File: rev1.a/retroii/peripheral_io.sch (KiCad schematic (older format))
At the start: 8 parts, among them J12 Peripheral Slot 0, J15 Peripheral Slot 4, J16 Peripheral Slot 1, J17 Peripheral Slot 5, J18 Peripheral Slot 2, J19 Peripheral Slot 6, J20 Peripheral Slot 3, J21 Peripheral Slot 7

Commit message: added card edge peripheral connector footprint and 3d model.
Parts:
- J12, J15, J16, J17, J18, J19, J20, J21: footprint (none) -> retroii_footprints:TE_5530841-5
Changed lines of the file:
@@
 F 0 "J12" H 3290 3515 50  0000 C CNN
 F 1 "Peripheral Slot 0" H 3140 915 50  0000 C CNN
-F 2 "" H 3160 2225 50  0001 C CNN
+F 2 "retroii_footprints:TE_5530841-5" H 3160 2225 50  0001 C CNN
 F 3 "~" H 3160 2225 50  0001 C CNN
 	1    3160 2225
@@
 F 0 "J16" H 4975 3515 50  0000 C CNN
 F 1 "Peripheral Slot 1" H 4825 915 50  0000 C CNN
-F 2 "" H 4845 2225 50  0001 C CNN
+F 2 "retroii_footprints:TE_5530841-5" H 4845 2225 50  0001 C CNN
 F 3 "~" H 4845 2225 50  0001 C CNN
 	1    4845 2225
@@
 F 0 "J18" H 6665 3515 50  0000 C CNN
 F 1 "Peripheral Slot 2" H 6515 915 50  0000 C CNN
-F 2 "" H 6535 2225 50  0001 C CNN
+F 2 "retroii_footprints:TE_5530841-5" H 6535 2225 50  0001 C CNN
 F 3 "~" H 6535 2225 50  0001 C CNN
 	1    6535 2225
@@
 F 0 "J20" H 8350 3515 50  0000 C CNN
 F 1 "Peripheral Slot 3" H 8200 915 50  0000 C CNN
-F 2 "" H 8220 2225 50  0001 C CNN
+F 2 "retroii_footprints:TE_5530841-5" H 8220 2225 50  0001 C CNN
 F 3 "~" H 8220 2225 50  0001 C CNN
 	1    8220 2225
@@
 F 0 "J15" H 3290 6390 50  0000 C CNN
 F 1 "Peripheral Slot 4" H 3140 3790 50  0000 C CNN
-F 2 "" H 3160 5100 50  0001 C CNN
+F 2 "retroii_footprints:TE_5530841-5" H 3160 5100 50  0001 C CNN
 F 3 "~" H 3160 5100 50  0001 C CNN
 	1    3160 5100
@@
 F 0 "J17" H 4975 6390 50  0000 C CNN
 F 1 "Peripheral Slot 5" H 4825 3790 50  0000 C CNN
-F 2 "" H 4845 5100 50  0001 C CNN
+F 2 "retroii_footprints:TE_5530841-5" H 4845 5100 50  0001 C CNN
 F 3 "~" H 4845 5100 50  0001 C CNN
 	1    4845 5100
@@
 F 0 "J19" H 6665 6390 50  0000 C CNN
 F 1 "Peripheral Slot 6" H 6515 3790 50  0000 C CNN
-F 2 "" H 6535 5100 50  0001 C CNN
+F 2 "retroii_footprints:TE_5530841-5" H 6535 5100 50  0001 C CNN
 F 3 "~" H 6535 5100 50  0001 C CNN
 	1    6535 5100
@@
 F 0 "J21" H 8350 6390 50  0000 C CNN
 F 1 "Peripheral Slot 7" H 8200 3790 50  0000 C CNN
-F 2 "" H 8220 5100 50  0001 C CNN
+F 2 "retroii_footprints:TE_5530841-5" H 8220 5100 50  0001 C CNN
 F 3 "~" H 8220 5100 50  0001 C CNN
 	1    8220 5100

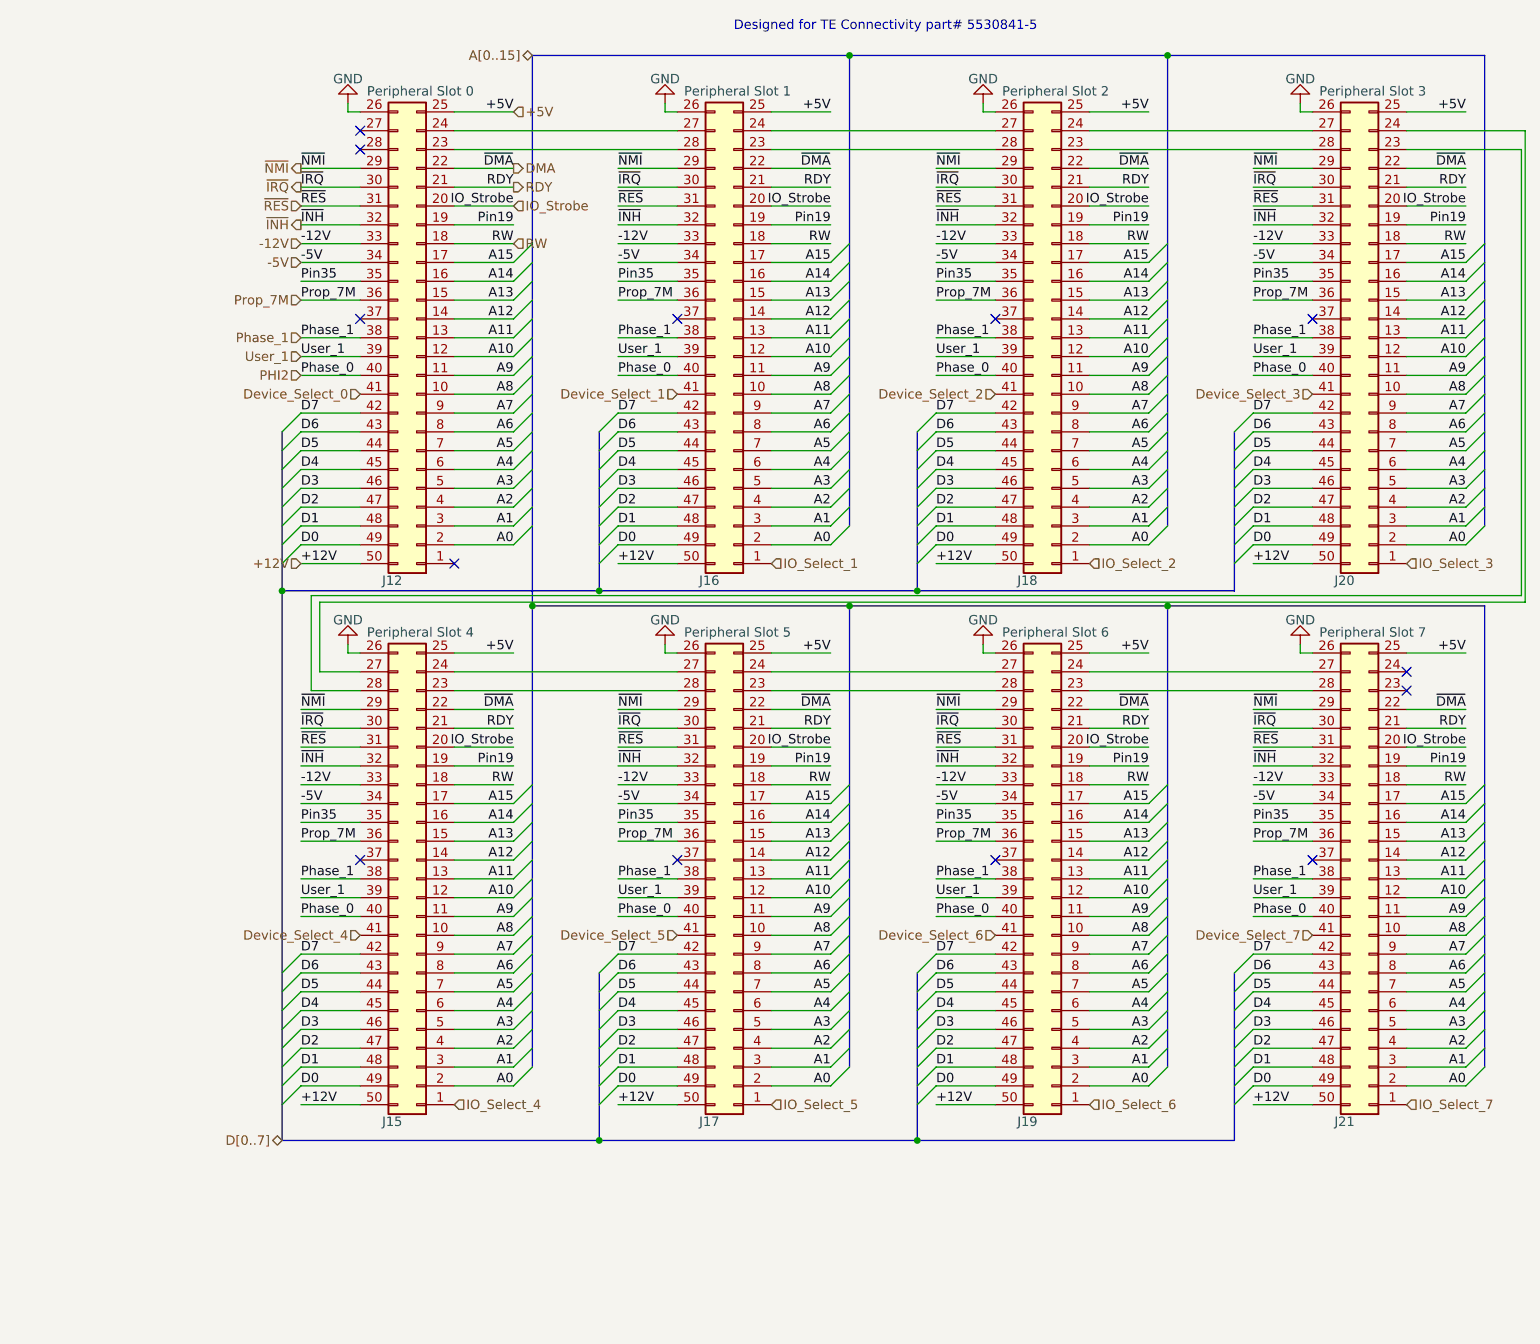
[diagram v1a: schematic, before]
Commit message: added optional bypass caps for peripheral slots
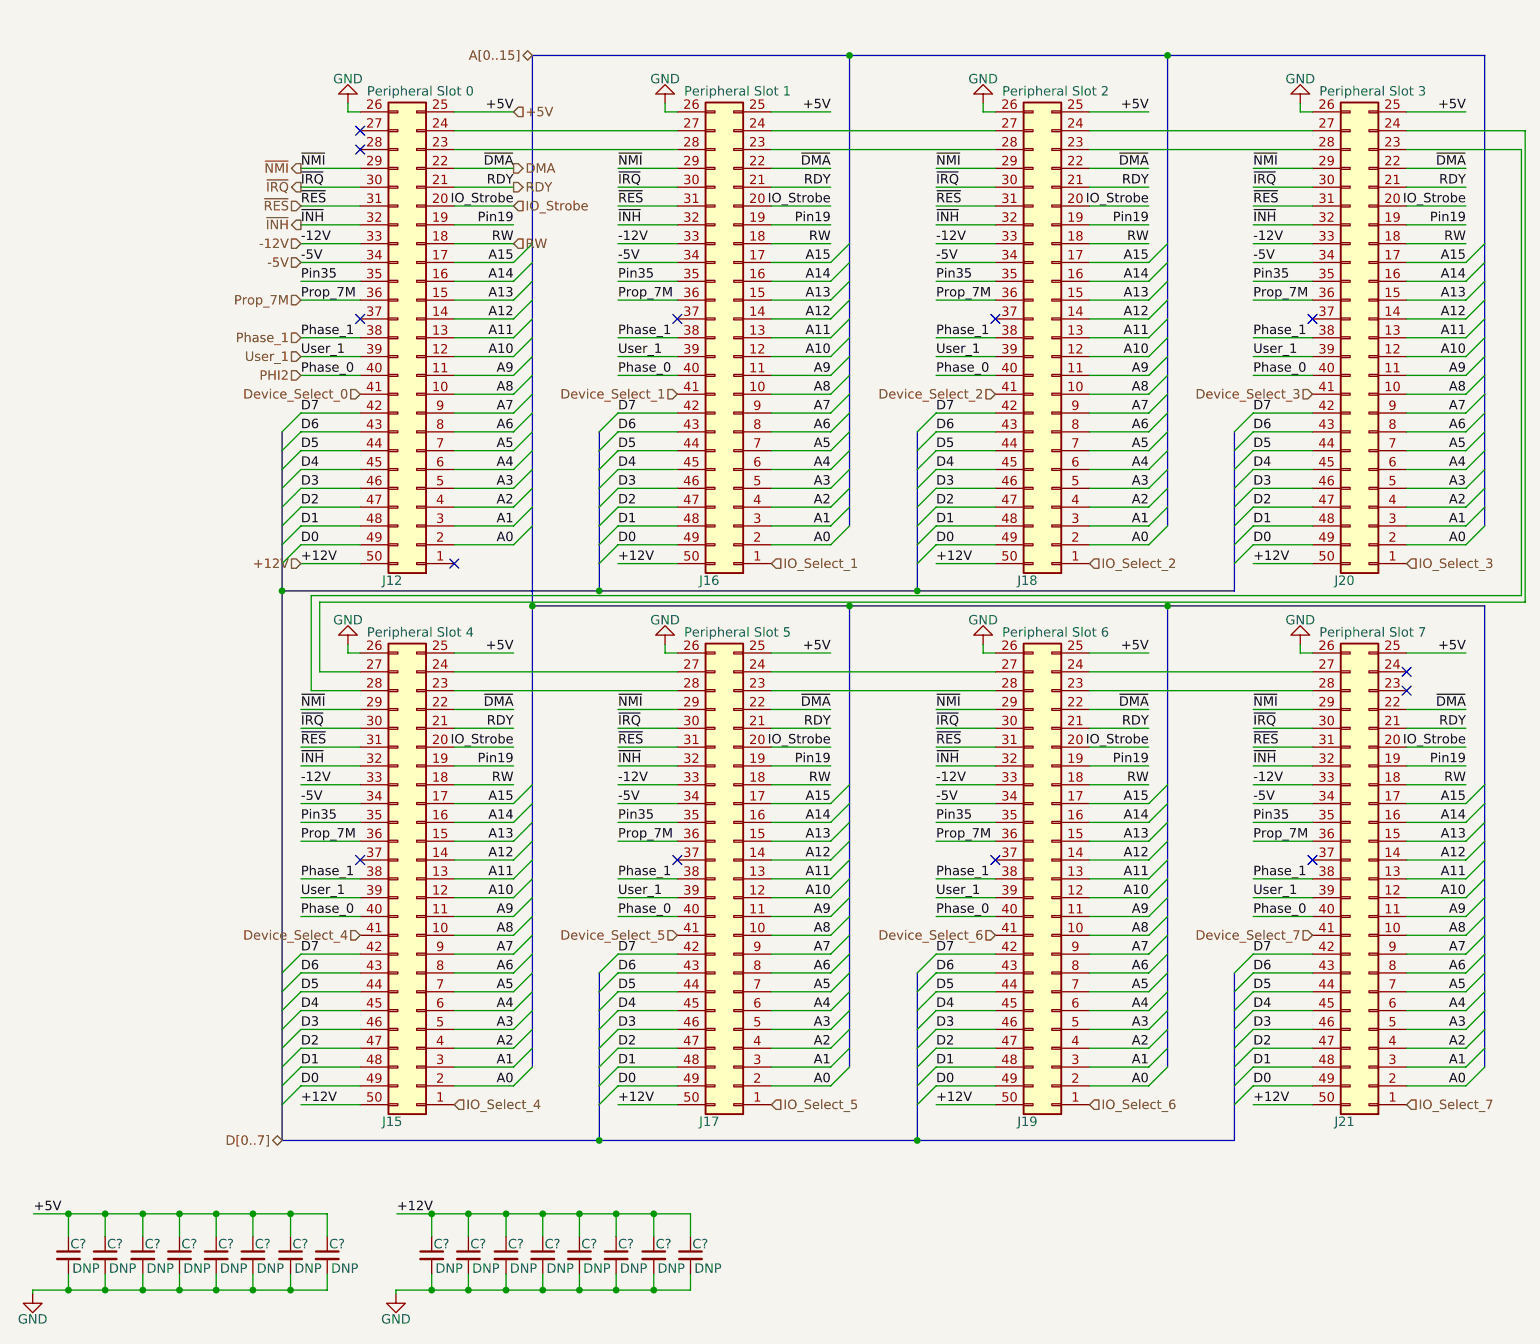
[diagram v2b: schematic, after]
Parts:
- added C? (x16): DNP, symbol Device:C_Small
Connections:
- net +12V: now also C?.1, C?.1, C?.1, C?.1, C?.1, C?.1, C?.1, C?.1
- net +5V: now also C?.1, C?.1, C?.1, C?.1, C?.1, C?.1, C?.1, C?.1
- net GND: now also C?.2, C?.2, C?.2, C?.2, C?.2, C?.2, C?.2, C?.2, C?.2, C?.2, C?.2, C?.2, C?.2, C?.2, C?.2, C?.2
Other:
- note removed: "Designed for TE Connectivity part# 5530841-5"

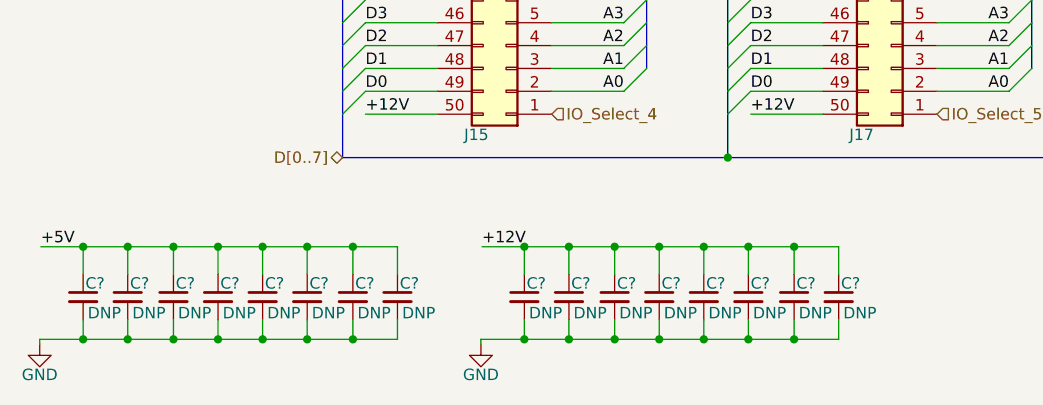
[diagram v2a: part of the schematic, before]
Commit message: added vga dsub-15 footprint and 3d model
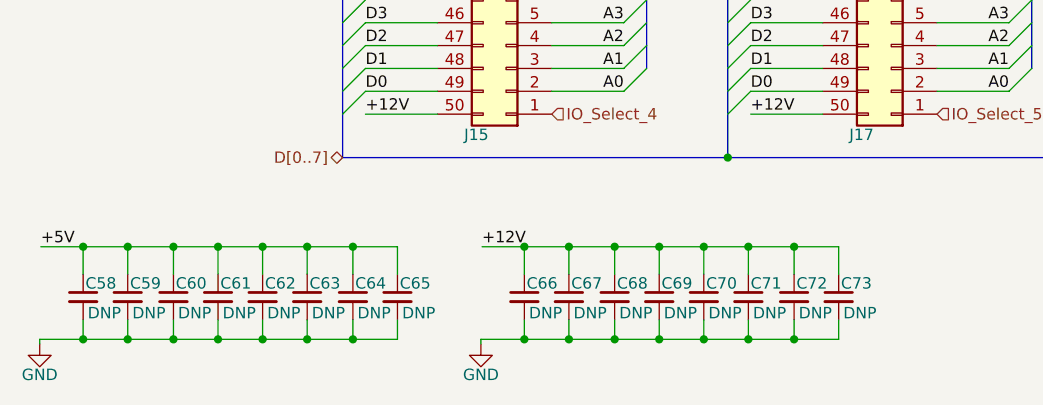
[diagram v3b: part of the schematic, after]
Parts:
- C58, C59, C60, C61, C62, C63, C64, C65, C66, C67, C68, C69, C70, C71, C72, C73: renamed from C?; footprint (none) -> retroii_footprints:C_Disc_D3.0mm_W2.0mm_P2.50mm
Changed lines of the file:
@@
 Prop_7M
 $Comp
-L Device:C_Small C?
+L Device:C_Small C58
 U 1 1 5CD43AB0
 P 1310 7100
-F 0 "C?" H 1320 7160 50  0000 L CNN
+F 0 "C58" H 1320 7160 50  0000 L CNN
 F 1 "DNP" H 1330 7030 50  0000 L CNN
-F 2 "" H 1310 7100 50  0001 C CNN
+F 2 "retroii_footprints:C_Disc_D3.0mm_W2.0mm_P2.50mm" H 1310 7100 50  0001 C CNN
 F 3 "~" H 1310 7100 50  0001 C CNN
 	1    1310 7100
@@
 $EndComp
 $Comp
-L Device:C_Small C?
+L Device:C_Small C59
 U 1 1 5CD476D4
 P 1505 7100
-F 0 "C?" H 1515 7160 50  0000 L CNN
+F 0 "C59" H 1515 7160 50  0000 L CNN
 F 1 "DNP" H 1525 7030 50  0000 L CNN
-F 2 "" H 1505 7100 50  0001 C CNN
+F 2 "retroii_footprints:C_Disc_D3.0mm_W2.0mm_P2.50mm" H 1505 7100 50  0001 C CNN
 F 3 "~" H 1505 7100 50  0001 C CNN
 	1    1505 7100
@@
 $EndComp
 $Comp
-L Device:C_Small C?
+L Device:C_Small C60
 U 1 1 5CD4865B
 P 1705 7100
-F 0 "C?" H 1715 7160 50  0000 L CNN
+F 0 "C60" H 1715 7160 50  0000 L CNN
 F 1 "DNP" H 1725 7030 50  0000 L CNN
-F 2 "" H 1705 7100 50  0001 C CNN
+F 2 "retroii_footprints:C_Disc_D3.0mm_W2.0mm_P2.50mm" H 1705 7100 50  0001 C CNN
 F 3 "~" H 1705 7100 50  0001 C CNN
 	1    1705 7100
@@
 $EndComp
 $Comp
-L Device:C_Small C?
+L Device:C_Small C61
 U 1 1 5CD48661
 P 1900 7100
-F 0 "C?" H 1910 7160 50  0000 L CNN
+F 0 "C61" H 1910 7160 50  0000 L CNN
 F 1 "DNP" H 1920 7030 50  0000 L CNN
-F 2 "" H 1900 7100 50  0001 C CNN
+F 2 "retroii_footprints:C_Disc_D3.0mm_W2.0mm_P2.50mm" H 1900 7100 50  0001 C CNN
 F 3 "~" H 1900 7100 50  0001 C CNN
 	1    1900 7100
@@
 $EndComp
 $Comp
-L Device:C_Small C?
+L Device:C_Small C62
 U 1 1 5CD8DC28
 P 2095 7100
-F 0 "C?" H 2105 7160 50  0000 L CNN
+F 0 "C62" H 2105 7160 50  0000 L CNN
 F 1 "DNP" H 2115 7030 50  0000 L CNN
-F 2 "" H 2095 7100 50  0001 C CNN
+F 2 "retroii_footprints:C_Disc_D3.0mm_W2.0mm_P2.50mm" H 2095 7100 50  0001 C CNN
 F 3 "~" H 2095 7100 50  0001 C CNN
 	1    2095 7100
@@
 $EndComp
 $Comp
-L Device:C_Small C?
+L Device:C_Small C63
 U 1 1 5CD8DC2E
 P 2290 7100
-F 0 "C?" H 2300 7160 50  0000 L CNN
+F 0 "C63" H 2300 7160 50  0000 L CNN
 F 1 "DNP" H 2310 7030 50  0000 L CNN
-F 2 "" H 2290 7100 50  0001 C CNN
+F 2 "retroii_footprints:C_Disc_D3.0mm_W2.0mm_P2.50mm" H 2290 7100 50  0001 C CNN
 F 3 "~" H 2290 7100 50  0001 C CNN
 	1    2290 7100
@@
 $EndComp
 $Comp
-L Device:C_Small C?
+L Device:C_Small C64
 U 1 1 5CD8DC34
 P 2490 7100
-F 0 "C?" H 2500 7160 50  0000 L CNN
+F 0 "C64" H 2500 7160 50  0000 L CNN
 F 1 "DNP" H 2510 7030 50  0000 L CNN
-F 2 "" H 2490 7100 50  0001 C CNN
+F 2 "retroii_footprints:C_Disc_D3.0mm_W2.0mm_P2.50mm" H 2490 7100 50  0001 C CNN
 F 3 "~" H 2490 7100 50  0001 C CNN
 	1    2490 7100
@@
 $EndComp
 $Comp
-L Device:C_Small C?
+L Device:C_Small C65
 U 1 1 5CD8DC3A
 P 2685 7100
-F 0 "C?" H 2695 7160 50  0000 L CNN
+F 0 "C65" H 2695 7160 50  0000 L CNN
 F 1 "DNP" H 2705 7030 50  0000 L CNN
-F 2 "" H 2685 7100 50  0001 C CNN
+F 2 "retroii_footprints:C_Disc_D3.0mm_W2.0mm_P2.50mm" H 2685 7100 50  0001 C CNN
 F 3 "~" H 2685 7100 50  0001 C CNN
 	1    2685 7100
@@
 	1120 7285 1120 7305
 $Comp
-L 6502Bootstrapper-cache:GND #PWR?
+L 6502Bootstrapper-cache:GND #PWR095
 U 1 1 5D2A2DB5
 P 1120 7305
-F 0 "#PWR?" H 1120 7055 50  0001 C CNN
+F 0 "#PWR095" H 1120 7055 50  0001 C CNN
 F 1 "GND" H 1120 7170 50  0000 C CNN
 F 2 "" H 1120 7305 60  0000 C CNN
@@
 $EndComp
 $Comp
-L Device:C_Small C?
+L Device:C_Small C66
 U 1 1 5D2A7028
 P 3240 7100
-F 0 "C?" H 3250 7160 50  0000 L CNN
+F 0 "C66" H 3250 7160 50  0000 L CNN
 F 1 "DNP" H 3260 7030 50  0000 L CNN
-F 2 "" H 3240 7100 50  0001 C CNN
+F 2 "retroii_footprints:C_Disc_D3.0mm_W2.0mm_P2.50mm" H 3240 7100 50  0001 C CNN
 F 3 "~" H 3240 7100 50  0001 C CNN
 	1    3240 7100
@@
 $EndComp
 $Comp
-L Device:C_Small C?
+L Device:C_Small C67
 U 1 1 5D2A702E
 P 3435 7100
-F 0 "C?" H 3445 7160 50  0000 L CNN
+F 0 "C67" H 3445 7160 50  0000 L CNN
 F 1 "DNP" H 3455 7030 50  0000 L CNN
-F 2 "" H 3435 7100 50  0001 C CNN
+F 2 "retroii_footprints:C_Disc_D3.0mm_W2.0mm_P2.50mm" H 3435 7100 50  0001 C CNN
 F 3 "~" H 3435 7100 50  0001 C CNN
 	1    3435 7100
@@
 $EndComp
 $Comp
-L Device:C_Small C?
+L Device:C_Small C68
 U 1 1 5D2A7034
 P 3635 7100
-F 0 "C?" H 3645 7160 50  0000 L CNN
+F 0 "C68" H 3645 7160 50  0000 L CNN
 F 1 "DNP" H 3655 7030 50  0000 L CNN
-F 2 "" H 3635 7100 50  0001 C CNN
+F 2 "retroii_footprints:C_Disc_D3.0mm_W2.0mm_P2.50mm" H 3635 7100 50  0001 C CNN
 F 3 "~" H 3635 7100 50  0001 C CNN
 	1    3635 7100
@@
 $EndComp
 $Comp
-L Device:C_Small C?
+L Device:C_Small C69
 U 1 1 5D2A703A
 P 3830 7100
-F 0 "C?" H 3840 7160 50  0000 L CNN
+F 0 "C69" H 3840 7160 50  0000 L CNN
 F 1 "DNP" H 3850 7030 50  0000 L CNN
-F 2 "" H 3830 7100 50  0001 C CNN
+F 2 "retroii_footprints:C_Disc_D3.0mm_W2.0mm_P2.50mm" H 3830 7100 50  0001 C CNN
 F 3 "~" H 3830 7100 50  0001 C CNN
 	1    3830 7100
@@
 $EndComp
 $Comp
-L Device:C_Small C?
+L Device:C_Small C70
 U 1 1 5D2A7040
 P 4025 7100
-F 0 "C?" H 4035 7160 50  0000 L CNN
+F 0 "C70" H 4035 7160 50  0000 L CNN
 F 1 "DNP" H 4045 7030 50  0000 L CNN
-F 2 "" H 4025 7100 50  0001 C CNN
+F 2 "retroii_footprints:C_Disc_D3.0mm_W2.0mm_P2.50mm" H 4025 7100 50  0001 C CNN
 F 3 "~" H 4025 7100 50  0001 C CNN
 	1    4025 7100
@@
 $EndComp
 $Comp
-L Device:C_Small C?
+L Device:C_Small C71
 U 1 1 5D2A7046
 P 4220 7100
-F 0 "C?" H 4230 7160 50  0000 L CNN
+F 0 "C71" H 4230 7160 50  0000 L CNN
 F 1 "DNP" H 4240 7030 50  0000 L CNN
-F 2 "" H 4220 7100 50  0001 C CNN
+F 2 "retroii_footprints:C_Disc_D3.0mm_W2.0mm_P2.50mm" H 4220 7100 50  0001 C CNN
 F 3 "~" H 4220 7100 50  0001 C CNN
 	1    4220 7100
@@
 $EndComp
 $Comp
-L Device:C_Small C?
+L Device:C_Small C72
 U 1 1 5D2A704C
 P 4420 7100
-F 0 "C?" H 4430 7160 50  0000 L CNN
+F 0 "C72" H 4430 7160 50  0000 L CNN
 F 1 "DNP" H 4440 7030 50  0000 L CNN
-F 2 "" H 4420 7100 50  0001 C CNN
+F 2 "retroii_footprints:C_Disc_D3.0mm_W2.0mm_P2.50mm" H 4420 7100 50  0001 C CNN
 F 3 "~" H 4420 7100 50  0001 C CNN
 	1    4420 7100
@@
 $EndComp
 $Comp
-L Device:C_Small C?
+L Device:C_Small C73
 U 1 1 5D2A7052
 P 4615 7100
-F 0 "C?" H 4625 7160 50  0000 L CNN
+F 0 "C73" H 4625 7160 50  0000 L CNN
 F 1 "DNP" H 4635 7030 50  0000 L CNN
-F 2 "" H 4615 7100 50  0001 C CNN
+F 2 "retroii_footprints:C_Disc_D3.0mm_W2.0mm_P2.50mm" H 4615 7100 50  0001 C CNN
 F 3 "~" H 4615 7100 50  0001 C CNN
 	1    4615 7100
@@
 	3050 7285 3050 7305
 $Comp
-L 6502Bootstrapper-cache:GND #PWR?
+L 6502Bootstrapper-cache:GND #PWR096
 U 1 1 5D2A7088
 P 3050 7305
-F 0 "#PWR?" H 3050 7055 50  0001 C CNN
+F 0 "#PWR096" H 3050 7055 50  0001 C CNN
 F 1 "GND" H 3050 7170 50  0000 C CNN
 F 2 "" H 3050 7305 60  0000 C CNN
